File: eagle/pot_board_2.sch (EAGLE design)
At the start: 18 parts, among them IC1 4067N, X2 22-23-2081

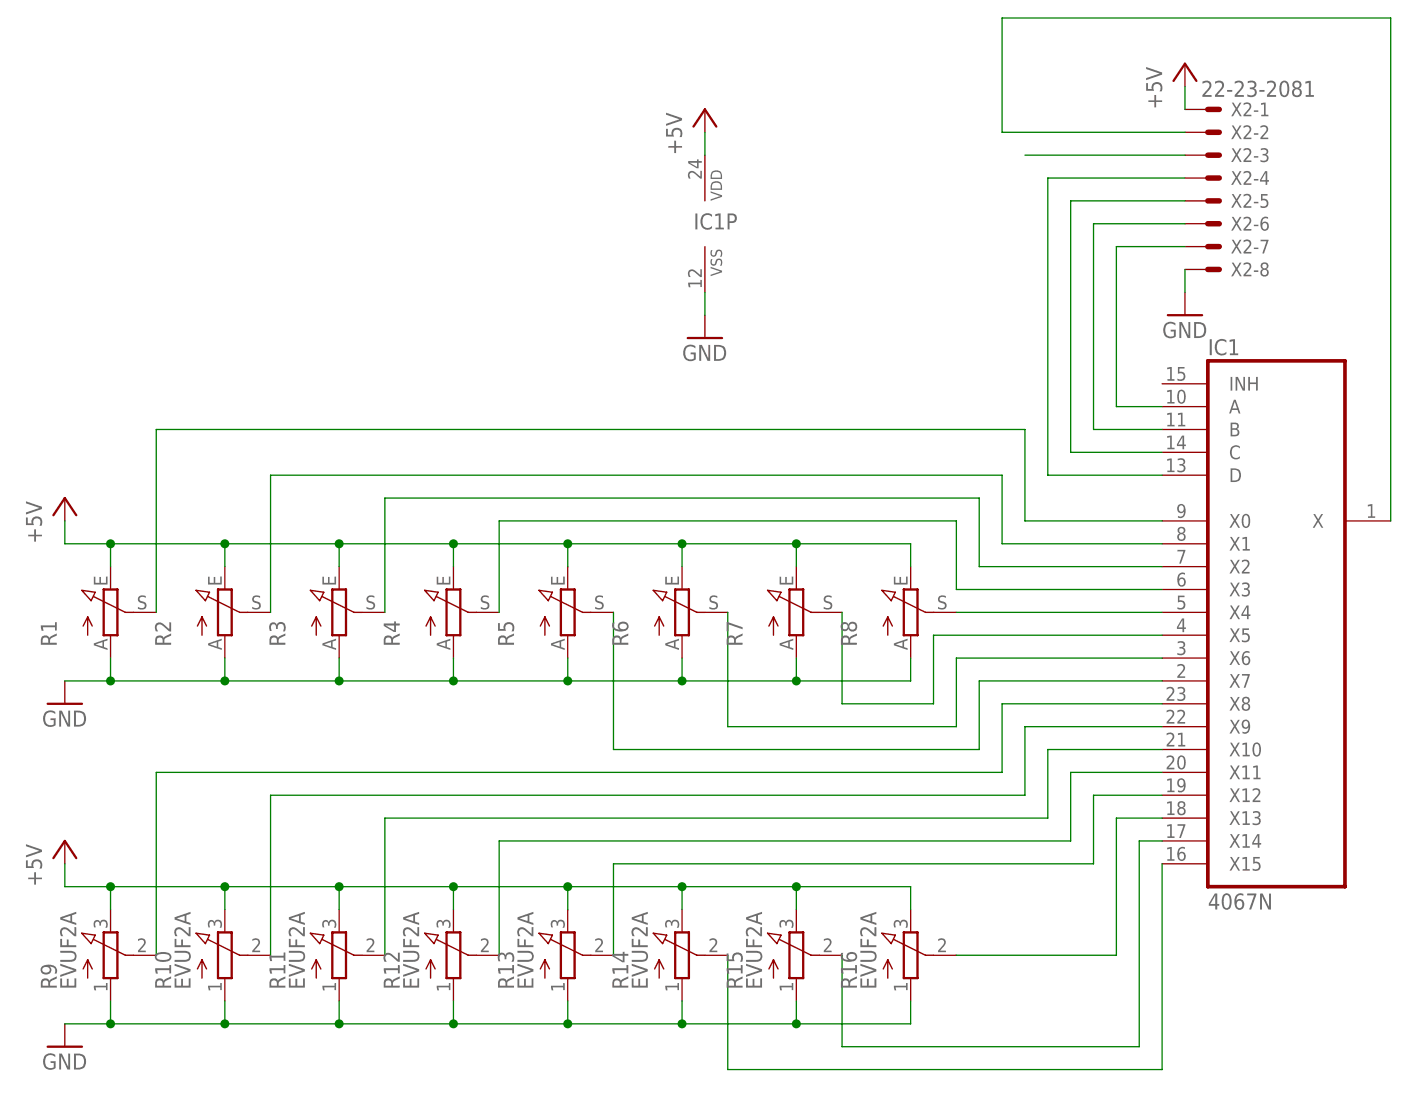
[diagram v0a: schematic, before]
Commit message: standard connector for display
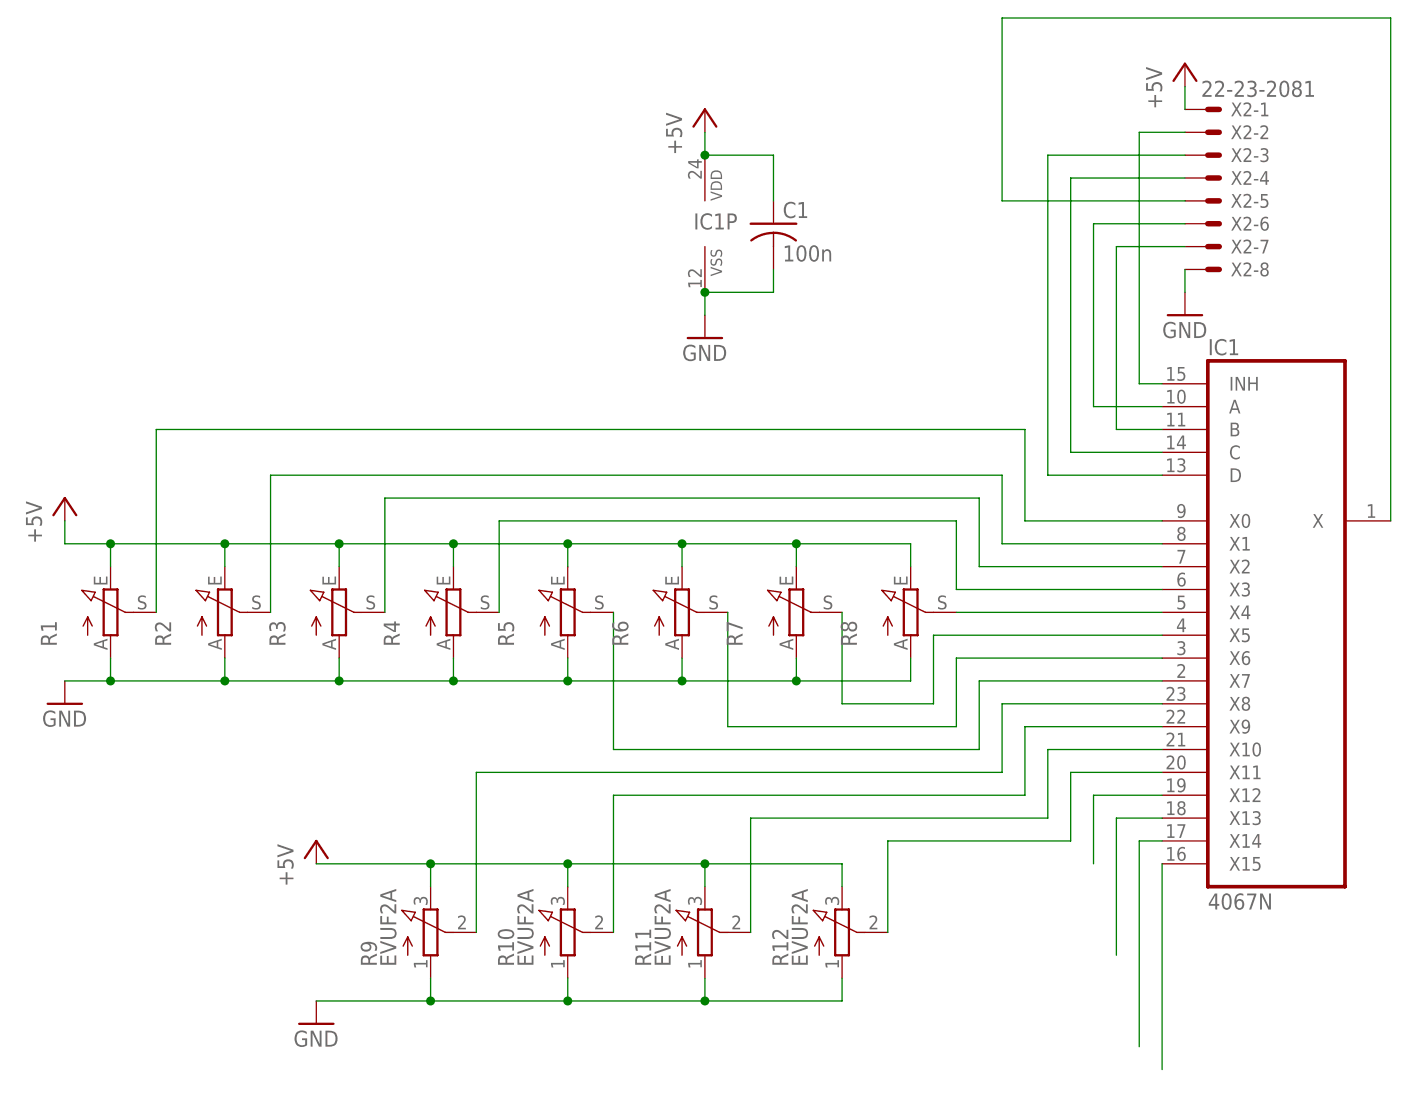
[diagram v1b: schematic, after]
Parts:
- removed R13, R14, R15, R16: EVUF2A, pot:EVUF2A
- added C1: 100n, rcl:C-US025-024X044
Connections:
- removed net N$16: X2-3.S
- new net N$9: IC1A.INH, X2-2.S
- net +5V: now also C1.1; no longer R13.E, R14.E, R15.E, R16.E
- net GND: now also C1.2; no longer R13.A, R14.A, R15.A, R16.A
- net N$12: now also IC1A.B; no longer IC1A.A
- net N$13: now also IC1A.A; no longer IC1A.B
- net N$14: now also X2-4.S; no longer X2-5.S
- net N$15: now also X2-3.S; no longer X2-4.S
- net N$17: now also X2-5.S; no longer X2-2.S
- net N$21: no longer R13.S
- net N$22: no longer R16.S
- net N$23: no longer R15.S
- net N$24: no longer R14.S
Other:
- moved on the sheet: R10, R11, R12, R9
